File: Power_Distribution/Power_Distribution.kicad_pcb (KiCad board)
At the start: 2 copper layers, 70 x 38 mm, 14 parts, among them J1 PWR Out, J2 GND Out

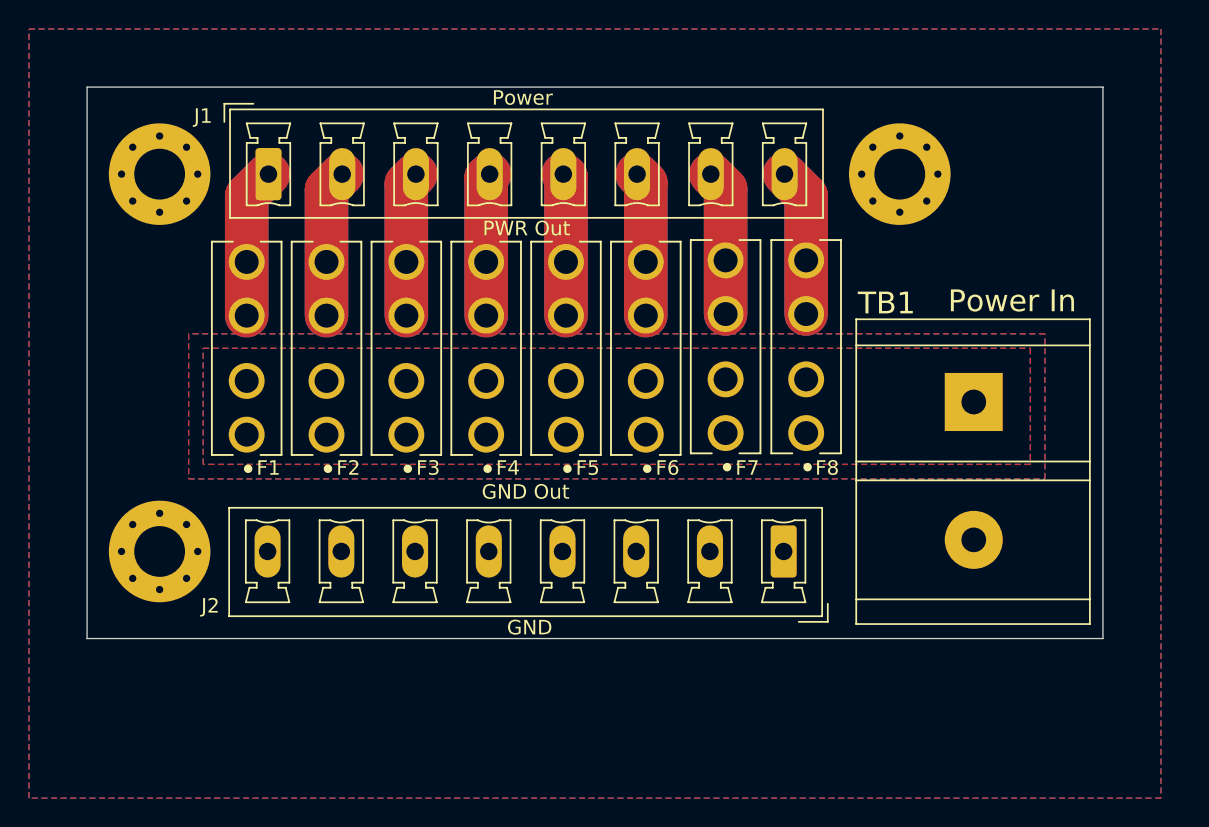
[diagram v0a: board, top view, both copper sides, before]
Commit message: Update Silkscreen and Added BOM
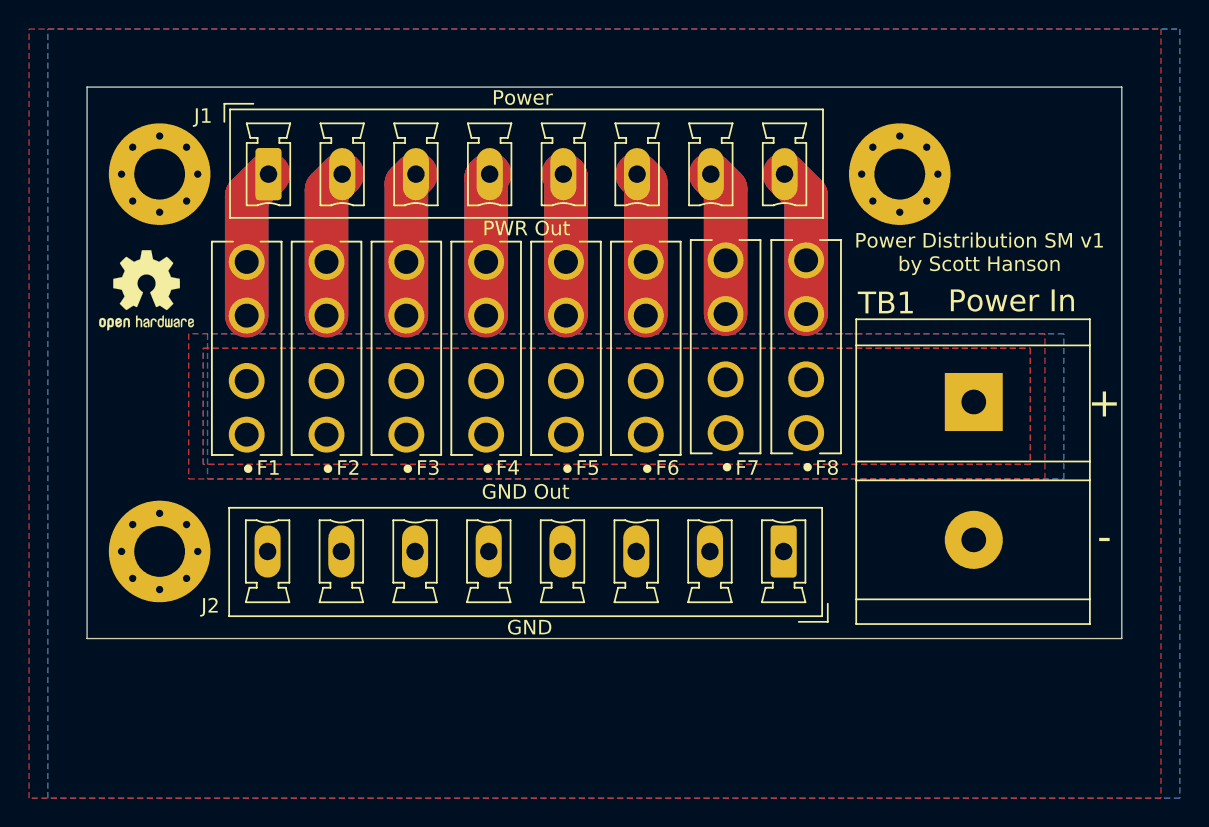
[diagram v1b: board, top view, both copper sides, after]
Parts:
- added REF**: OSHW-Logo2_7.3x6mm_SilkScreen, Symbol:OSHW-Logo2_7.3x6mm_SilkScreen, F.Cu at (95.1, 93.0)
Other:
- board size 70 x 38 mm -> 71.3 x 38 mm
- board text added: "Power Distribution SM v1 by Scott Hanson"

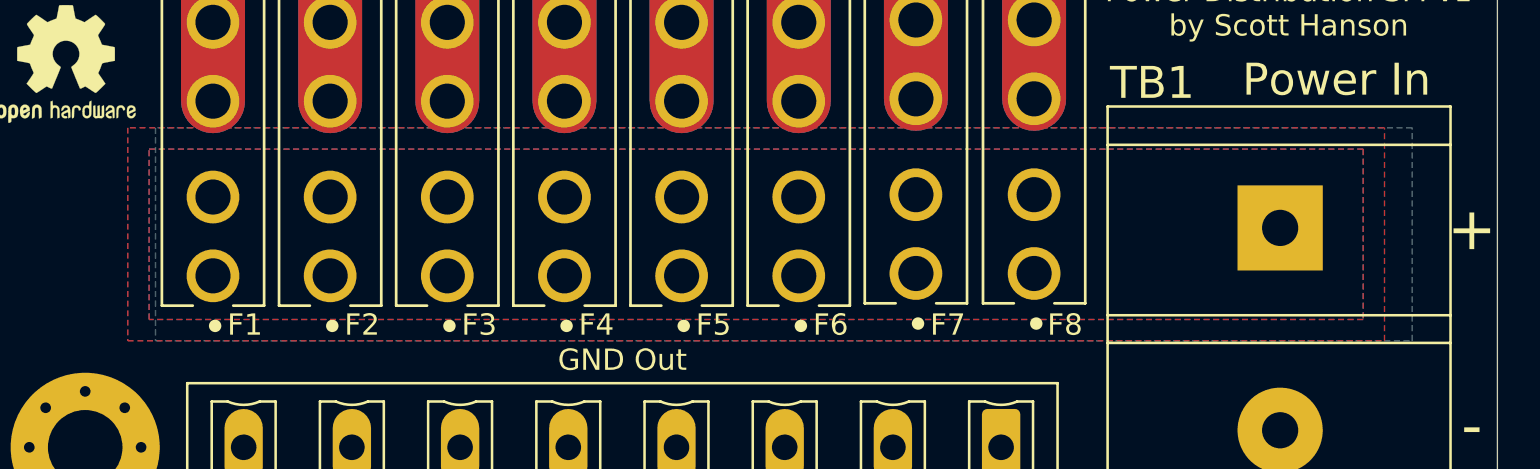
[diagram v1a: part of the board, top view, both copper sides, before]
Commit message: added power distros
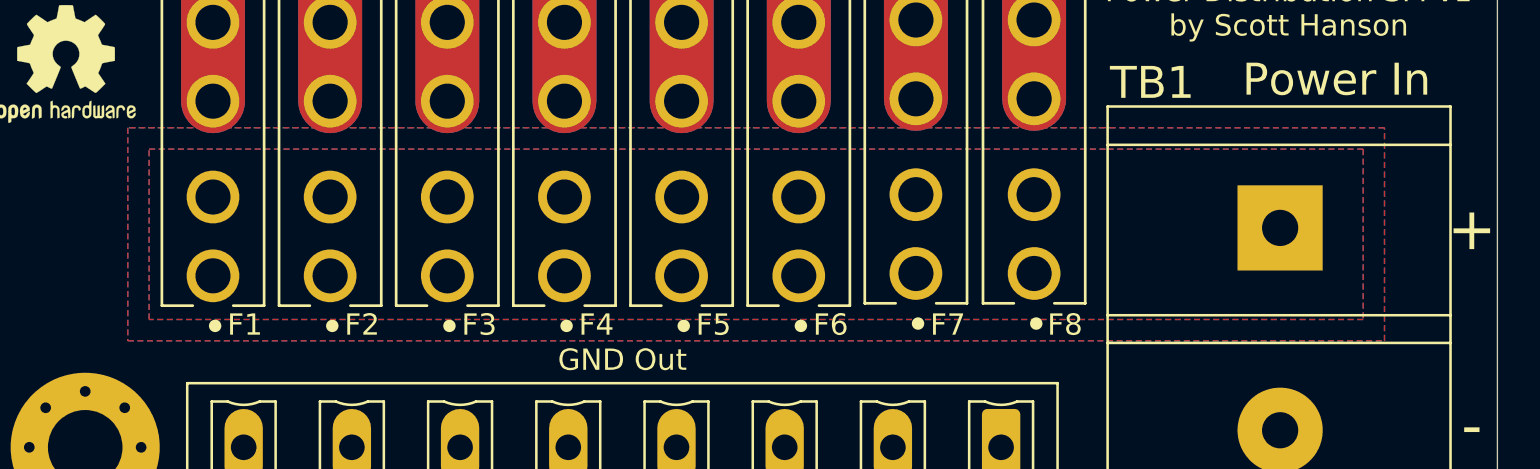
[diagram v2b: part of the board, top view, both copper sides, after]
